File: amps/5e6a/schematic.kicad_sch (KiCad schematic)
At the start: 62 parts, among them T3 part not legible

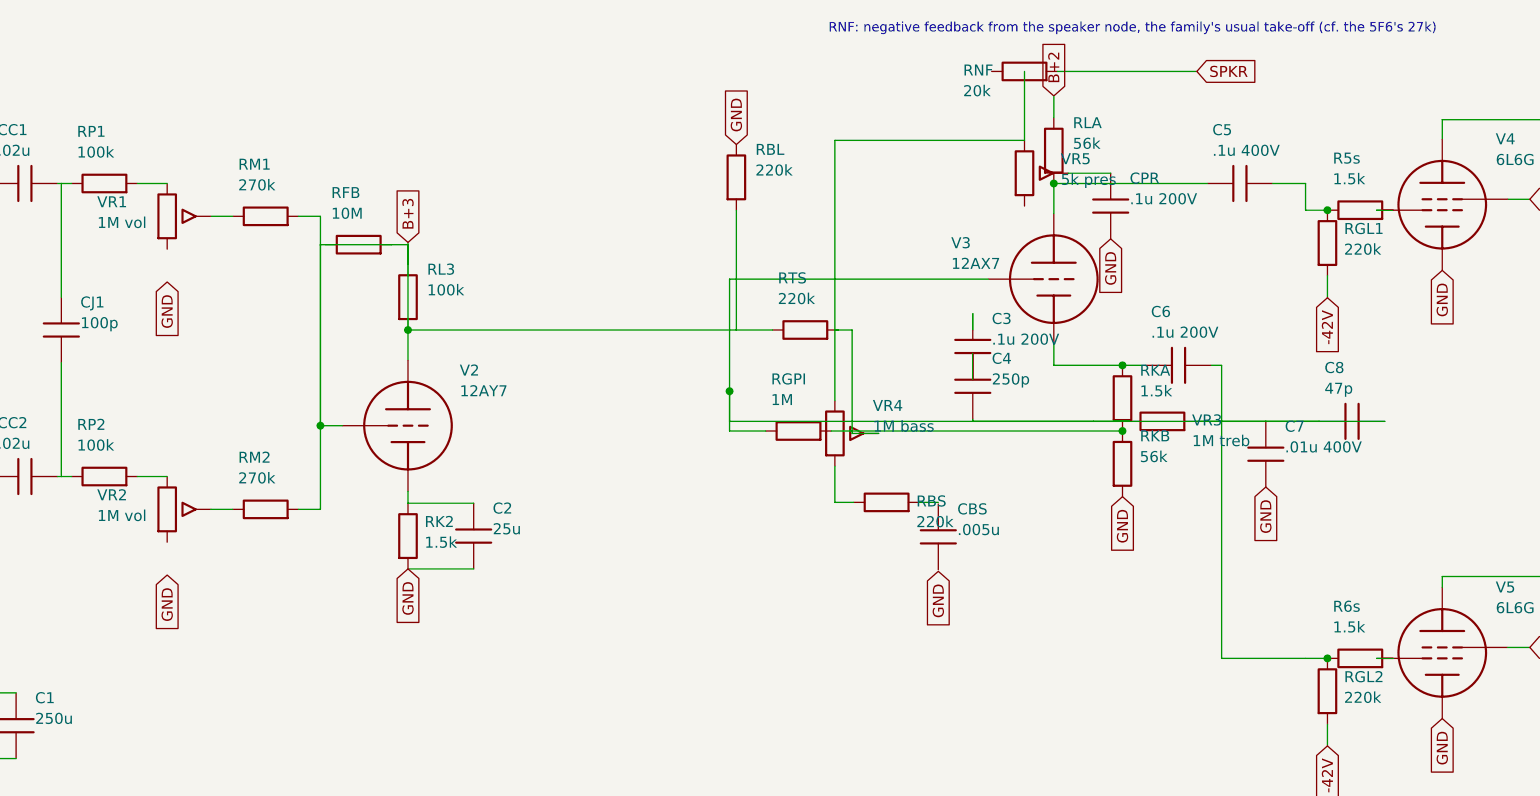
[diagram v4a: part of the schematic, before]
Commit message: Fix: schematic wiring on the tweed family, jtm45 and 6161
- pot cold lugs: s.gnd() sat 3.81 mm below cx:POT pin 3 on nine sheets
  (19 pins); every flag now lands on the lug
- retyped coordinates replaced by helper returns (5e5a OT pins alone freed
  nine pins; 5d3 V3 cathode, 5f10 RKB, 5e6a CBS, 5f2a dropper, grid leaks)
- shorts only verify_schematic_nets could see: 5e3 cathode bus through V4's
  screen pin (B+2 tied to the cathodes), C7 through RG6A, PI leak through
  RGPI, C8 on the cathode not the tail; 5f10 the same RGPI/C7 pair; 5e5a
  presence feed down the tube column; 5e6a RFB loop through RL3
- three dated waivers: two-terminal rheostat far lugs (5e6a VR5, 6161 VR3/VR4)

Co-Authored-By: Claude Fable 5.1 <noreply@anthropic.com>
Claude-Session: https://claude.ai/code/session_01KBMfdh37HmCL2iWcBiL5J1
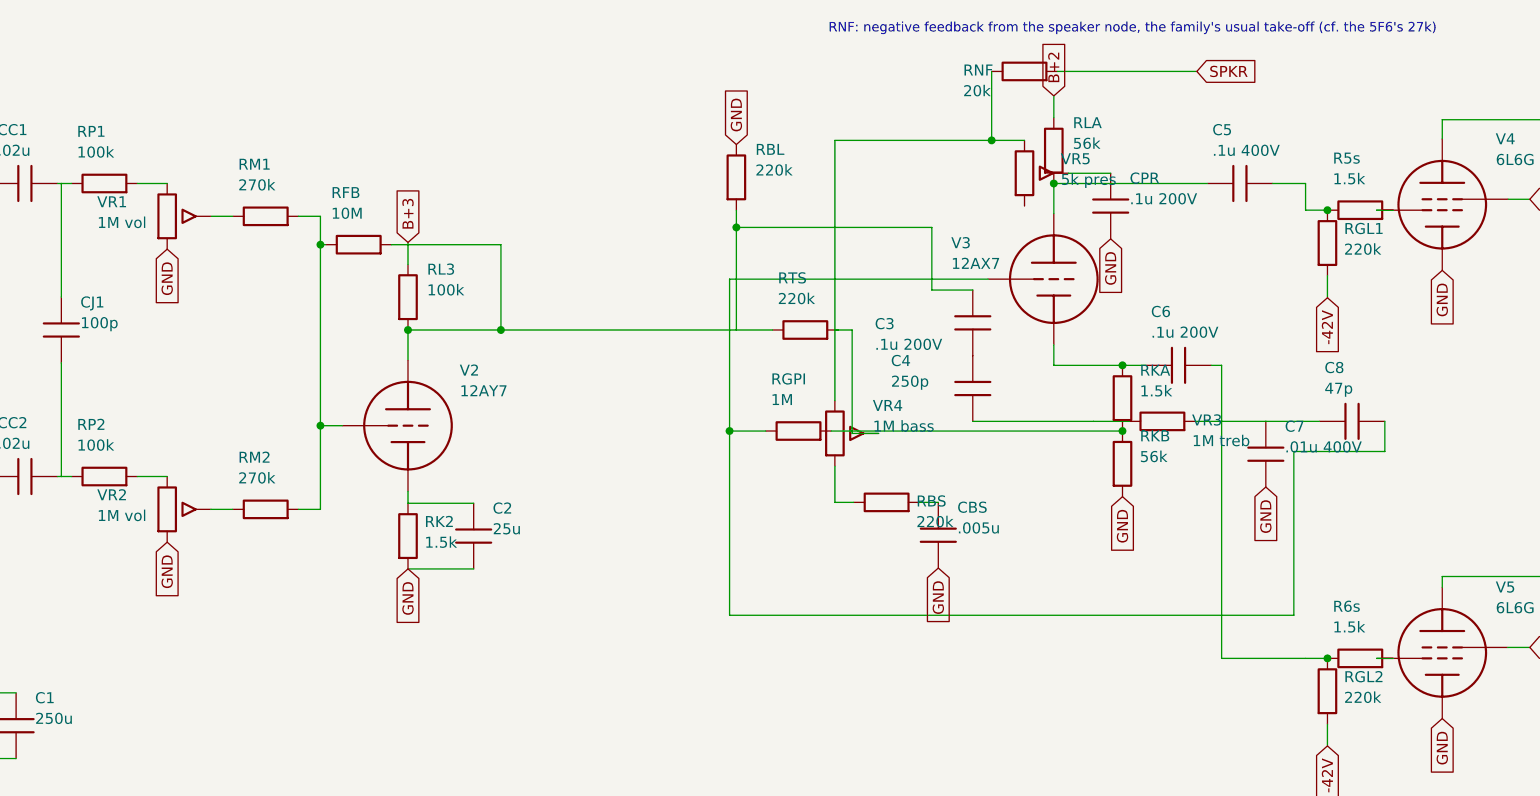
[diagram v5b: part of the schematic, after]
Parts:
- removed C3: .1u 200V, symbol cx:C
- removed RB1: 3.3k, symbol cx:R
- removed RD2: 10k, symbol cx:R
- added C12: 16u, symbol cx:C
- added C7: .01u 400V, symbol cx:C
- added D1: SEL, symbol cx:DIODE_SS
- C3: renamed from VR3; value 1M treb -> .1u 200V; symbol cx:R -> cx:C
- RB1: renamed from D1; value SEL -> 3.3k; symbol cx:DIODE_SS -> cx:R
- RD2: renamed from C12; value 16u -> 10k; symbol cx:C -> cx:R
- VR3: renamed from C7; value .01u 400V -> 1M treb; symbol cx:C -> cx:R
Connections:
- net -42V: now also RB1.2
- net B+2: now also C12.1
- net B+3: now also RD2.2; no longer RBL.2, RFB.1, RFB.2, RL3.2, RM1.2, RM2.2, RTS.1, V2.1 (P)
- net GND: now also CBS.2, VR1.3, VR2.3, C12.2, C7.2; no longer RD2.2, VR3.2
- net HT_B: now also D1.1 (A); no longer RB1.1 (A)
- net at CBS.1: now also RBS.2
- net at RTS.2, VR4.1, VR4.2 (W)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: now also RNF.1
- net at C4.1: now also C3.2
- new net: D1.2 (K), RB1.1
- new net: C8.2, RGPI.1, V3.2 (G)
- new net: RFB.1, RM1.2, RM2.2
- new net: C3.1, RBL.2, RFB.2, RL3.2, RTS.1, V2.1 (P)
- new net: C7.1, C8.1, VR3.2
- new net: C4.2, VR3.1
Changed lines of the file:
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@@
     (property "Reference" "VR1" (at 65.0404 33.54 0) (effects (font (size 1.27 1.27)) (justify left)))
     (property "Value" "1M vol" (at 65.0404 35.94 0) (effects (font (size 1.27 1.27)) (justify left))))
-  (global_label "GND" (shape input) (at 73.1616 42.8 270)
+  (global_label "GND" (shape input) (at 73.1616 38.99 270)
     (effects (font (size 1.27 1.27)) (justify right)))
   (wire (pts (xy 78.2416 35.18) (xy 80.7816 35.18))
@@
     (property "Reference" "VR2" (at 65.0404 67.54 0) (effects (font (size 1.27 1.27)) (justify left)))
     (property "Value" "1M vol" (at 65.0404 69.94 0) (effects (font (size 1.27 1.27)) (justify left))))
-  (global_label "GND" (shape input) (at 73.1616 76.8 270)
+  (global_label "GND" (shape input) (at 73.1616 72.99 270)
     (effects (font (size 1.27 1.27)) (justify right)))
   (wire (pts (xy 78.2416 69.18) (xy 80.7816 69.18))
@@
     (property "Reference" "RL3" (at 103.302 41.36 0) (effects (font (size 1.27 1.27)) (justify left)))
     (property "Value" "100k" (at 103.302 43.76 0) (effects (font (size 1.27 1.27)) (justify left))))
-  (wire (pts (xy 101.102 40.75) (xy 101.102 38.47))
-    (stroke (width 0) (type default)))
-  (wire (pts (xy 101.102 38.47) (xy 101.102 38.21))
+  (wire (pts (xy 101.102 40.75) (xy 101.102 38.21))
     (stroke (width 0) (type default)))
   (global_label "B+3" (shape input) (at 101.102 38.21 90)
     (effects (font (size 1.27 1.27)) (justify left)))
-  (wire (pts (xy 101.102 48.37) (xy 101.102 40.75))
-    (stroke (width 0) (type default)))
-  (wire (pts (xy 101.102 40.75) (xy 101.102 38.47))
-    (stroke (width 0) (type default)))
-  (wire (pts (xy 101.102 38.47) (xy 99.1916 38.47))
-    (stroke (width 0) (type default)))
-  (wire (pts (xy 99.1916 38.47) (xy 91.5716 38.47))
-    (stroke (width 0) (type default)))
-  (wire (pts (xy 91.5716 38.47) (xy 90.9416 38.47))
-    (stroke (width 0) (type default)))
-  (wire (pts (xy 90.9416 38.47) (xy 90.9416 59.47))
-    (stroke (width 0) (type default)))
   (symbol (lib_id "cx:R") (at 95.3816 38.47 90) (unit 1)
     (in_bom yes) (on_board yes)
     (property "Reference" "RFB" (at 92.1816 32.47 270) (effects (font (size 1.27 1.27)) (justify left)))
     (property "Value" "10M" (at 92.1816 34.87 270) (effects (font (size 1.27 1.27)) (justify left))))
-  (wire (pts (xy 101.102 48.37) (xy 139.202 48.37))
+  (wire (pts (xy 111.882 48.37) (xy 111.882 38.47))
+    (stroke (width 0) (type default)))
+  (junction (at 111.882 48.37) (diameter 0) (color 0 0 0 0))
+  (wire (pts (xy 99.1916 38.47) (xy 111.882 38.47))
+    (stroke (width 0) (type default)))
+  (wire (pts (xy 90.9416 38.47) (xy 91.5716 38.47))
+    (stroke (width 0) (type default)))
+  (junction (at 90.9416 38.47) (diameter 0) (color 0 0 0 0))
+  (wire (pts (xy 101.102 48.37) (xy 111.882 48.37))
+    (stroke (width 0) (type default)))
+  (wire (pts (xy 111.882 48.37) (xy 139.202 48.37))
     (stroke (width 0) (type default)))
   (junction (at 101.102 48.37) (diameter 0) (color 0 0 0 0))
-  (wire (pts (xy 139.202 48.37) (xy 139.202 34.47))
+  (wire (pts (xy 139.202 48.37) (xy 139.202 36.47))
+    (stroke (width 0) (type default)))
+  (wire (pts (xy 139.202 36.47) (xy 139.202 34.47))
     (stroke (width 0) (type default)))
   (symbol (lib_id "cx:R") (at 139.202 30.66 0) (unit 1)
@@
   (wire (pts (xy 160.442 68.37) (xy 162.632 68.37))
     (stroke (width 0) (type default)))
-  (symbol (lib_id "cx:C") (at 162.632 72.37 0) (unit 1)
-    (in_bom yes) (on_board yes)
-    (property "Reference" "CBS" (at 164.832 69.17 0) (effects (font (size 1.27 1.27)) (justify left)))
-    (property "Value" ".005u" (at 164.832 71.57 0) (effects (font (size 1.27 1.27)) (justify left))))
-  (global_label "GND" (shape input) (at 162.632 76.37 270)
+  (symbol (lib_id "cx:C") (at 162.632 72.18 0) (unit 1)
+    (in_bom yes) (on_board yes)
+    (property "Reference" "CBS" (at 164.832 68.98 0) (effects (font (size 1.27 1.27)) (justify left)))
+    (property "Value" ".005u" (at 164.832 71.38 0) (effects (font (size 1.27 1.27)) (justify left))))
+  (global_label "GND" (shape input) (at 162.632 75.99 270)
     (effects (font (size 1.27 1.27)) (justify right)))
   (symbol (lib_id "cx:POT") (at 172.632 30.18 0) (unit 1)
@@
     (property "Reference" "VR5" (at 176.834 28.54 0) (effects (font (size 1.27 1.27)) (justify left)))
     (property "Value" "5k pres" (at 176.834 30.94 0) (effects (font (size 1.27 1.27)) (justify left))))
-  (wire (pts (xy 150.632 26.37) (xy 172.632 26.37))
+  (wire (pts (xy 150.632 26.37) (xy 168.822 26.37))
+    (stroke (width 0) (type default)))
+  (wire (pts (xy 168.822 26.37) (xy 172.632 26.37))
     (stroke (width 0) (type default)))
   (wire (pts (xy 177.712 30.18) (xy 182.632 30.18))
@@
     (property "Reference" "RNF" (at 165.502 18.254 270) (effects (font (size 1.27 1.27)) (justify left)))
     (property "Value" "20k" (at 165.502 20.654 270) (effects (font (size 1.27 1.27)) (justify left))))
-  (wire (pts (xy 172.632 26.37) (xy 172.632 18.37))
-    (stroke (width 0) (type default)))
+  (wire (pts (xy 168.822 26.37) (xy 168.822 18.37))
+    (stroke (width 0) (type default)))
+  (junction (at 168.822 26.37) (diameter 0) (color 0 0 0 0))
   (wire (pts (xy 176.442 18.37) (xy 192.632 18.37))
     (stroke (width 0) (type default)))
@@
   (text "RNF: negative feedback from the speaker node, the family's usual take-off (cf. the 5F6's 27k)" (at 149.882 13.47 0)
     (effects (font (size 1.1 1.1)) (justify left)))
-  (wire (pts (xy 166.632 48.37) (xy 166.632 46.47))
-    (stroke (width 0) (type default)))
-  (symbol (lib_id "cx:C") (at 166.632 50.28 0) (unit 1)
-    (in_bom yes) (on_board yes)
-    (property "Reference" "C3" (at 168.832 47.08 0) (effects (font (size 1.27 1.27)) (justify left)))
-    (property "Value" ".1u 200V" (at 168.832 49.48 0) (effects (font (size 1.27 1.27)) (justify left))))
-  (wire (pts (xy 166.632 54.09) (xy 166.632 51.09))
-    (stroke (width 0) (type default)))
-  (symbol (lib_id "cx:C") (at 166.632 54.9 0) (unit 1)
-    (in_bom yes) (on_board yes)
-    (property "Reference" "C4" (at 168.832 51.7 0) (effects (font (size 1.27 1.27)) (justify left)))
-    (property "Value" "250p" (at 168.832 54.1 0) (effects (font (size 1.27 1.27)) (justify left))))
-  (wire (pts (xy 166.632 58.71) (xy 166.632 58.97))
-    (stroke (width 0) (type default)))
+  (wire (pts (xy 139.202 36.47) (xy 161.882 36.47))
+    (stroke (width 0) (type default)))
+  (junction (at 139.202 36.47) (diameter 0) (color 0 0 0 0))
+  (wire (pts (xy 161.882 36.47) (xy 161.882 43.73))
+    (stroke (width 0) (type default)))
+  (wire (pts (xy 161.882 43.73) (xy 166.632 43.73))
+    (stroke (width 0) (type default)))
+  (symbol (lib_id "cx:C") (at 166.632 47.54 0) (unit 1)
+    (in_bom yes) (on_board yes)
+    (property "Reference" "C3" (at 155.259 47.678 0) (effects (font (size 1.27 1.27)) (justify left)))
+    (property "Value" ".1u 200V" (at 155.259 50.078 0) (effects (font (size 1.27 1.27)) (justify left))))
+  (symbol (lib_id "cx:C") (at 166.632 55.16 0) (unit 1)
+    (in_bom yes) (on_board yes)
+    (property "Reference" "C4" (at 157.132 51.96 0) (effects (font (size 1.27 1.27)) (justify left)))
+    (property "Value" "250p" (at 157.132 54.36 0) (effects (font (size 1.27 1.27)) (justify left))))
   (wire (pts (xy 166.632 58.97) (xy 180.632 58.97))
     (stroke (width 0) (type default)))
@@
     (property "Reference" "V3" (at 164.127 38.29 0) (effects (font (size 1.27 1.27)) (justify left)))
     (property "Value" "12AX7" (at 164.127 40.69 0) (effects (font (size 1.27 1.27)) (justify left))))
-  (wire (pts (xy 214.442 58.97) (xy 206.822 58.97))
-    (stroke (width 0) (type default)))
-  (wire (pts (xy 206.822 58.97) (xy 200.632 58.97))
-    (stroke (width 0) (type default)))
-  (wire (pts (xy 200.632 58.97) (xy 192.442 58.97))
-    (stroke (width 0) (type default)))
-  (wire (pts (xy 192.442 58.97) (xy 184.822 58.97))
-    (stroke (width 0) (type default)))
-  (wire (pts (xy 184.822 58.97) (xy 180.632 58.97))
-    (stroke (width 0) (type default)))
-  (wire (pts (xy 180.632 58.97) (xy 166.632 58.97))
-    (stroke (width 0) (type default)))
-  (wire (pts (xy 166.632 58.97) (xy 138.412 58.97))
-    (stroke (width 0) (type default)))
-  (wire (pts (xy 138.412 58.97) (xy 138.412 55.47))
-    (stroke (width 0) (type default)))
-  (wire (pts (xy 138.412 55.47) (xy 138.412 42.47))
+  (wire (pts (xy 214.442 58.97) (xy 214.442 62.47))
+    (stroke (width 0) (type default)))
+  (wire (pts (xy 214.442 62.47) (xy 203.882 62.47))
+    (stroke (width 0) (type default)))
+  (wire (pts (xy 203.882 62.47) (xy 203.882 81.47))
+    (stroke (width 0) (type default)))
+  (wire (pts (xy 203.882 81.47) (xy 138.412 81.47))
+    (stroke (width 0) (type default)))
+  (wire (pts (xy 138.412 81.47) (xy 138.412 60.09))
+    (stroke (width 0) (type default)))
+  (wire (pts (xy 138.412 60.09) (xy 138.412 42.47))
     (stroke (width 0) (type default)))
   (wire (pts (xy 138.412 42.47) (xy 168.412 42.47))
@@
   (global_label "GND" (shape input) (at 184.002 67.71 270)
     (effects (font (size 1.27 1.27)) (justify right)))
-  (wire (pts (xy 138.412 55.47) (xy 138.412 58.97))
-    (stroke (width 0) (type default)))
-  (wire (pts (xy 138.412 58.97) (xy 138.412 60.09))
-    (stroke (width 0) (type default)))
-  (junction (at 138.412 55.47) (diameter 0) (color 0 0 0 0))
+  (junction (at 138.412 60.09) (diameter 0) (color 0 0 0 0))
   (symbol (lib_id "cx:R") (at 146.412 60.09 90) (unit 1)
     (in_bom yes) (on_board yes)
